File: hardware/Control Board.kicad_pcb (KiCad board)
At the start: 2 copper layers, 68.4 x 53.1 mm, 42 parts, among them J1 Conn_FTDI, J2 SOLAR, M1 MOTOR, Q1 IRF7105PbF, Q2 BC817W, Q3 BC817W, Q4 IRF7105PbF, SW1 SW_Push, SW2 SW_Push, SW3 SW_Push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

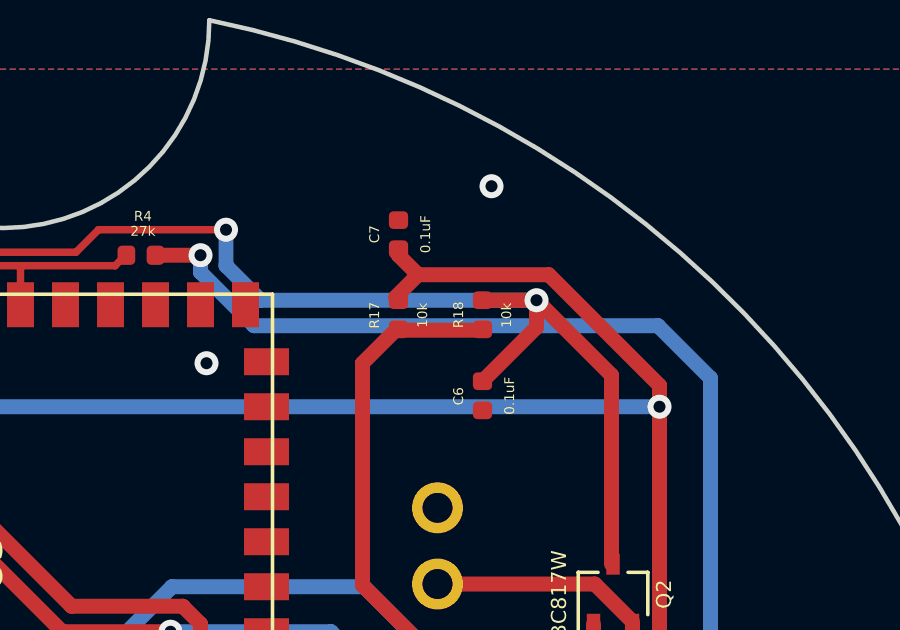
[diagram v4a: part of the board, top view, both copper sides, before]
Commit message: Placing the pull ups on the programmer
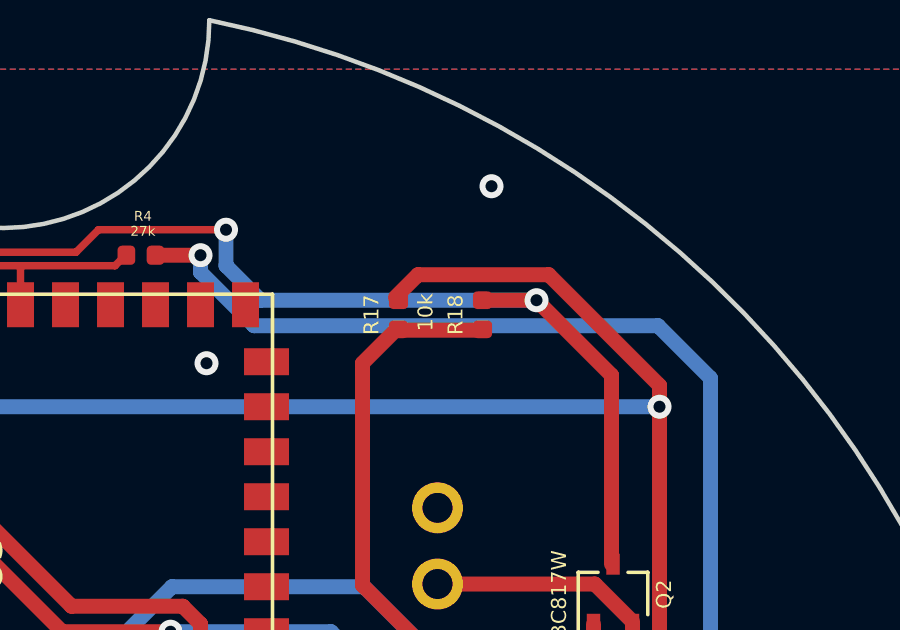
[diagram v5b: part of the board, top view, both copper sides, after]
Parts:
- removed C6, C7: 0.1uF, Capacitor_SMD:C_0402_1005Metric
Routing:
- net EN: track 53.0 -> 49.5 mm
- net IO0: track 72.7 -> 71.6 mm
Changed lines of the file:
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@@
     (thickness 1.6)
     (drawings 57)
-    (tracks 275)
+    (tracks 268)
     (zones 0)
-    (modules 42)
+    (modules 40)
     (nets 54)
   )
@@
     (tags resistor)
     (attr smd)
-    (fp_text reference R17 (at -0.015 -0.8 90) (layer F.SilkS)
-      (effects (font (size 0.33 0.33) (thickness 0.0825)))
-    )
-    (fp_text value 10k (at -0.015 0.8 90) (layer F.SilkS)
-      (effects (font (size 0.33 0.33) (thickness 0.0825)))
+    (fp_text reference R17 (at 0 -0.9 90) (layer F.SilkS)
+      (effects (font (size 0.5 0.5) (thickness 0.125)))
+    )
+    (fp_text value 10k (at 0.085 0.9 90) (layer F.SilkS)
+      (effects (font (size 0.5 0.5) (thickness 0.125)))
     )
     (fp_line (start 0.93 0.47) (end -0.93 0.47) (layer F.CrtYd) (width 0.05))
@@
     (tags resistor)
     (attr smd)
-    (fp_text reference R18 (at 0 -0.8 90) (layer F.SilkS)
-      (effects (font (size 0.33 0.33) (thickness 0.0825)))
-    )
-    (fp_text value 10k (at -0.015 0.8 90) (layer F.SilkS)
-      (effects (font (size 0.33 0.33) (thickness 0.0825)))
+    (fp_text reference R18 (at 0 -0.9 90) (layer F.SilkS)
+      (effects (font (size 0.5 0.5) (thickness 0.125)))
+    )
+    (fp_text value 10k (at 0.085 0.9 90) (layer B.Paste)
+      (effects (font (size 0.5 0.5) (thickness 0.125)))
     )
     (fp_text user %R (at 0 0 90) (layer F.Fab)
@@
       (net 3 +3V3))
     (model ${KISYS3DMOD}/Resistor_SMD.3dshapes/R_0402_1005Metric.wrl
-      (at (xyz 0 0 0))
-      (scale (xyz 1 1 1))
-      (rotate (xyz 0 0 0))
-    )
-  )
-  (module Capacitor_SMD:C_0402_1005Metric (layer F.Cu)
-    (at 125 109.385 270)
-    (descr "Capacitor SMD 0402 (1005 Metric), square (rectangular) end terminal, IPC_7351 nominal, (Body size source: http://www.tortai-tech.com/upload/download/2011102023233369053.pdf), generated with kicad-footprint-generator")
-    (tags capacitor)
-    (attr smd)
-    (fp_text reference C6 (at 0.015 0.8 90) (layer F.SilkS)
-      (effects (font (size 0.33 0.33) (thickness 0.0825)))
-    )
-    (fp_text value 0.1uF (at 0 -0.9 90) (layer F.SilkS)
-      (effects (font (size 0.33 0.33) (thickness 0.0825)))
-    )
-    (fp_line (start 0.93 0.47) (end -0.93 0.47) (layer F.CrtYd) (width 0.05))
-    (fp_line (start 0.93 -0.47) (end 0.93 0.47) (layer F.CrtYd) (width 0.05))
-    (fp_line (start -0.93 -0.47) (end 0.93 -0.47) (layer F.CrtYd) (width 0.05))
-    (fp_line (start -0.93 0.47) (end -0.93 -0.47) (layer F.CrtYd) (width 0.05))
-    (fp_line (start 0.5 0.25) (end -0.5 0.25) (layer F.Fab) (width 0.1))
-    (fp_line (start 0.5 -0.25) (end 0.5 0.25) (layer F.Fab) (width 0.1))
-    (fp_line (start -0.5 -0.25) (end 0.5 -0.25) (layer F.Fab) (width 0.1))
-    (fp_line (start -0.5 0.25) (end -0.5 -0.25) (layer F.Fab) (width 0.1))
-    (fp_text user %R (at 0 0 90) (layer F.Fab)
-      (effects (font (size 0.25 0.25) (thickness 0.04)))
-    )
-    (pad 1 smd roundrect (at -0.485 0 270) (size 0.59 0.64) (layers F.Cu F.Paste F.Mask) (roundrect_rratio 0.25)
-      (net 9 EN))
-    (pad 2 smd roundrect (at 0.485 0 270) (size 0.59 0.64) (layers F.Cu F.Paste F.Mask) (roundrect_rratio 0.25)
-      (net 1 GND))
-    (model ${KISYS3DMOD}/Capacitor_SMD.3dshapes/C_0402_1005Metric.wrl
-      (at (xyz 0 0 0))
-      (scale (xyz 1 1 1))
-      (rotate (xyz 0 0 0))
-    )
-  )
-  (module Capacitor_SMD:C_0402_1005Metric (layer F.Cu)
-    (at 122.2 104.015 90)
-    (descr "Capacitor SMD 0402 (1005 Metric), square (rectangular) end terminal, IPC_7351 nominal, (Body size source: http://www.tortai-tech.com/upload/download/2011102023233369053.pdf), generated with kicad-footprint-generator")
-    (tags capacitor)
-    (attr smd)
-    (fp_text reference C7 (at 0.015 -0.8 90) (layer F.SilkS)
-      (effects (font (size 0.33 0.33) (thickness 0.0825)))
-    )
-    (fp_text value 0.1uF (at 0.015 0.9 90) (layer F.SilkS)
-      (effects (font (size 0.33 0.33) (thickness 0.0825)))
-    )
-    (fp_text user %R (at 0 0 90) (layer F.Fab)
-      (effects (font (size 0.25 0.25) (thickness 0.04)))
-    )
-    (fp_line (start -0.5 0.25) (end -0.5 -0.25) (layer F.Fab) (width 0.1))
-    (fp_line (start -0.5 -0.25) (end 0.5 -0.25) (layer F.Fab) (width 0.1))
-    (fp_line (start 0.5 -0.25) (end 0.5 0.25) (layer F.Fab) (width 0.1))
-    (fp_line (start 0.5 0.25) (end -0.5 0.25) (layer F.Fab) (width 0.1))
-    (fp_line (start -0.93 0.47) (end -0.93 -0.47) (layer F.CrtYd) (width 0.05))
-    (fp_line (start -0.93 -0.47) (end 0.93 -0.47) (layer F.CrtYd) (width 0.05))
-    (fp_line (start 0.93 -0.47) (end 0.93 0.47) (layer F.CrtYd) (width 0.05))
-    (fp_line (start 0.93 0.47) (end -0.93 0.47) (layer F.CrtYd) (width 0.05))
-    (pad 2 smd roundrect (at 0.485 0 90) (size 0.59 0.64) (layers F.Cu F.Paste F.Mask) (roundrect_rratio 0.25)
-      (net 1 GND))
-    (pad 1 smd roundrect (at -0.485 0 90) (size 0.59 0.64) (layers F.Cu F.Paste F.Mask) (roundrect_rratio 0.25)
-      (net 10 IO0))
-    (model ${KISYS3DMOD}/Capacitor_SMD.3dshapes/C_0402_1005Metric.wrl
       (at (xyz 0 0 0))
       (scale (xyz 1 1 1))
@@
   (segment (start 106.4 104.6) (end 111.449999 104.6) (width 0.25) (layer F.Cu) (net 9))
   (segment (start 125 106.2) (end 126.8 106.2) (width 0.5) (layer F.Cu) (net 9))
-  (segment (start 126.8 107.1) (end 126.8 106.2) (width 0.5) (layer F.Cu) (net 9))
-  (segment (start 125 108.9) (end 126.8 107.1) (width 0.5) (layer F.Cu) (net 9))
   (via (at 130.9 109.75) (size 0.8) (drill 0.4) (layers F.Cu B.Cu) (net 10))
   (via (at 97.6 118.9) (size 0.8) (drill 0.4) (layers F.Cu B.Cu) (net 10))
@@
   (segment (start 130.9 109.75) (end 130.9 109.041998) (width 0.5) (layer F.Cu) (net 10))
   (segment (start 122.850001 105.349999) (end 122.1 106.1) (width 0.5) (layer F.Cu) (net 10))
-  (segment (start 122.2 104.699998) (end 122.850001 105.349999) (width 0.5) (layer F.Cu) (net 10))
-  (segment (start 122.2 104.5) (end 122.2 104.699998) (width 0.5) (layer F.Cu) (net 10))
   (segment (start 128.7 119.87) (end 128.7 121.8) (width 0.5) (layer F.Cu) (net 11))
   (segment (start 123.5 125.82) (end 124.58 125.82) (width 0.5) (layer F.Cu) (net 11))

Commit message: Broke the pcb during a merge.
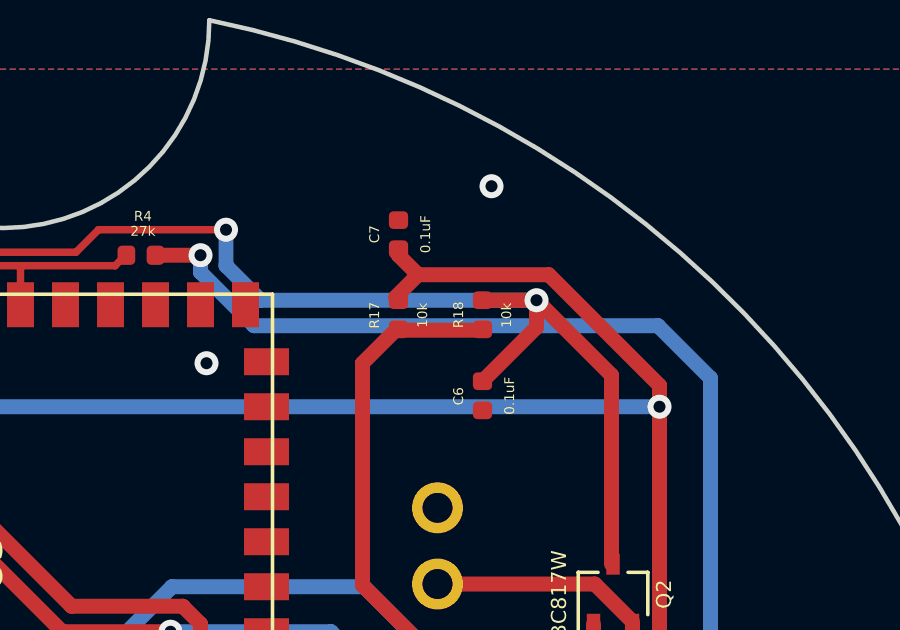
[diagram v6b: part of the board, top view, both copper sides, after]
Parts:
- added C6: 0.1uF, Capacitor_SMD:C_0402_1005Metric, F.Cu at (125.0, 109.4)
- added C7: 0.1uF, Capacitor_SMD:C_0402_1005Metric, F.Cu at (122.2, 104.0)
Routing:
- net EN: track 49.5 -> 53.0 mm
- net IO0: track 71.6 -> 72.7 mm
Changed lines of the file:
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@@
     (thickness 1.6)
     (drawings 57)
-    (tracks 268)
+    (tracks 275)
     (zones 0)
-    (modules 40)
+    (modules 42)
     (nets 54)
   )
@@
     (tags resistor)
     (attr smd)
-    (fp_text reference R17 (at 0 -0.9 90) (layer F.SilkS)
-      (effects (font (size 0.5 0.5) (thickness 0.125)))
-    )
-    (fp_text value 10k (at 0.085 0.9 90) (layer F.SilkS)
-      (effects (font (size 0.5 0.5) (thickness 0.125)))
+    (fp_text reference R17 (at -0.015 -0.8 90) (layer F.SilkS)
+      (effects (font (size 0.33 0.33) (thickness 0.0825)))
+    )
+    (fp_text value 10k (at -0.015 0.8 90) (layer F.SilkS)
+      (effects (font (size 0.33 0.33) (thickness 0.0825)))
     )
     (fp_line (start 0.93 0.47) (end -0.93 0.47) (layer F.CrtYd) (width 0.05))
@@
     (tags resistor)
     (attr smd)
-    (fp_text reference R18 (at 0 -0.9 90) (layer F.SilkS)
-      (effects (font (size 0.5 0.5) (thickness 0.125)))
-    )
-    (fp_text value 10k (at 0.085 0.9 90) (layer B.Paste)
-      (effects (font (size 0.5 0.5) (thickness 0.125)))
+    (fp_text reference R18 (at 0 -0.8 90) (layer F.SilkS)
+      (effects (font (size 0.33 0.33) (thickness 0.0825)))
+    )
+    (fp_text value 10k (at -0.015 0.8 90) (layer F.SilkS)
+      (effects (font (size 0.33 0.33) (thickness 0.0825)))
     )
     (fp_text user %R (at 0 0 90) (layer F.Fab)
@@
       (net 3 +3V3))
     (model ${KISYS3DMOD}/Resistor_SMD.3dshapes/R_0402_1005Metric.wrl
+      (at (xyz 0 0 0))
+      (scale (xyz 1 1 1))
+      (rotate (xyz 0 0 0))
+    )
+  )
+  (module Capacitor_SMD:C_0402_1005Metric (layer F.Cu)
+    (at 125 109.385 270)
+    (descr "Capacitor SMD 0402 (1005 Metric), square (rectangular) end terminal, IPC_7351 nominal, (Body size source: http://www.tortai-tech.com/upload/download/2011102023233369053.pdf), generated with kicad-footprint-generator")
+    (tags capacitor)
+    (attr smd)
+    (fp_text reference C6 (at 0.015 0.8 90) (layer F.SilkS)
+      (effects (font (size 0.33 0.33) (thickness 0.0825)))
+    )
+    (fp_text value 0.1uF (at 0 -0.9 90) (layer F.SilkS)
+      (effects (font (size 0.33 0.33) (thickness 0.0825)))
+    )
+    (fp_line (start 0.93 0.47) (end -0.93 0.47) (layer F.CrtYd) (width 0.05))
+    (fp_line (start 0.93 -0.47) (end 0.93 0.47) (layer F.CrtYd) (width 0.05))
+    (fp_line (start -0.93 -0.47) (end 0.93 -0.47) (layer F.CrtYd) (width 0.05))
+    (fp_line (start -0.93 0.47) (end -0.93 -0.47) (layer F.CrtYd) (width 0.05))
+    (fp_line (start 0.5 0.25) (end -0.5 0.25) (layer F.Fab) (width 0.1))
+    (fp_line (start 0.5 -0.25) (end 0.5 0.25) (layer F.Fab) (width 0.1))
+    (fp_line (start -0.5 -0.25) (end 0.5 -0.25) (layer F.Fab) (width 0.1))
+    (fp_line (start -0.5 0.25) (end -0.5 -0.25) (layer F.Fab) (width 0.1))
+    (fp_text user %R (at 0 0 90) (layer F.Fab)
+      (effects (font (size 0.25 0.25) (thickness 0.04)))
+    )
+    (pad 1 smd roundrect (at -0.485 0 270) (size 0.59 0.64) (layers F.Cu F.Paste F.Mask) (roundrect_rratio 0.25)
+      (net 9 EN))
+    (pad 2 smd roundrect (at 0.485 0 270) (size 0.59 0.64) (layers F.Cu F.Paste F.Mask) (roundrect_rratio 0.25)
+      (net 1 GND))
+    (model ${KISYS3DMOD}/Capacitor_SMD.3dshapes/C_0402_1005Metric.wrl
+      (at (xyz 0 0 0))
+      (scale (xyz 1 1 1))
+      (rotate (xyz 0 0 0))
+    )
+  )
+  (module Capacitor_SMD:C_0402_1005Metric (layer F.Cu)
+    (at 122.2 104.015 90)
+    (descr "Capacitor SMD 0402 (1005 Metric), square (rectangular) end terminal, IPC_7351 nominal, (Body size source: http://www.tortai-tech.com/upload/download/2011102023233369053.pdf), generated with kicad-footprint-generator")
+    (tags capacitor)
+    (attr smd)
+    (fp_text reference C7 (at 0.015 -0.8 90) (layer F.SilkS)
+      (effects (font (size 0.33 0.33) (thickness 0.0825)))
+    )
+    (fp_text value 0.1uF (at 0.015 0.9 90) (layer F.SilkS)
+      (effects (font (size 0.33 0.33) (thickness 0.0825)))
+    )
+    (fp_text user %R (at 0 0 90) (layer F.Fab)
+      (effects (font (size 0.25 0.25) (thickness 0.04)))
+    )
+    (fp_line (start -0.5 0.25) (end -0.5 -0.25) (layer F.Fab) (width 0.1))
+    (fp_line (start -0.5 -0.25) (end 0.5 -0.25) (layer F.Fab) (width 0.1))
+    (fp_line (start 0.5 -0.25) (end 0.5 0.25) (layer F.Fab) (width 0.1))
+    (fp_line (start 0.5 0.25) (end -0.5 0.25) (layer F.Fab) (width 0.1))
+    (fp_line (start -0.93 0.47) (end -0.93 -0.47) (layer F.CrtYd) (width 0.05))
+    (fp_line (start -0.93 -0.47) (end 0.93 -0.47) (layer F.CrtYd) (width 0.05))
+    (fp_line (start 0.93 -0.47) (end 0.93 0.47) (layer F.CrtYd) (width 0.05))
+    (fp_line (start 0.93 0.47) (end -0.93 0.47) (layer F.CrtYd) (width 0.05))
+    (pad 2 smd roundrect (at 0.485 0 90) (size 0.59 0.64) (layers F.Cu F.Paste F.Mask) (roundrect_rratio 0.25)
+      (net 1 GND))
+    (pad 1 smd roundrect (at -0.485 0 90) (size 0.59 0.64) (layers F.Cu F.Paste F.Mask) (roundrect_rratio 0.25)
+      (net 10 IO0))
+    (model ${KISYS3DMOD}/Capacitor_SMD.3dshapes/C_0402_1005Metric.wrl
       (at (xyz 0 0 0))
       (scale (xyz 1 1 1))
@@
   (segment (start 106.4 104.6) (end 111.449999 104.6) (width 0.25) (layer F.Cu) (net 9))
   (segment (start 125 106.2) (end 126.8 106.2) (width 0.5) (layer F.Cu) (net 9))
+  (segment (start 126.8 107.1) (end 126.8 106.2) (width 0.5) (layer F.Cu) (net 9))
+  (segment (start 125 108.9) (end 126.8 107.1) (width 0.5) (layer F.Cu) (net 9))
   (via (at 130.9 109.75) (size 0.8) (drill 0.4) (layers F.Cu B.Cu) (net 10))
   (via (at 97.6 118.9) (size 0.8) (drill 0.4) (layers F.Cu B.Cu) (net 10))
@@
   (segment (start 130.9 109.75) (end 130.9 109.041998) (width 0.5) (layer F.Cu) (net 10))
   (segment (start 122.850001 105.349999) (end 122.1 106.1) (width 0.5) (layer F.Cu) (net 10))
+  (segment (start 122.2 104.699998) (end 122.850001 105.349999) (width 0.5) (layer F.Cu) (net 10))
+  (segment (start 122.2 104.5) (end 122.2 104.699998) (width 0.5) (layer F.Cu) (net 10))
   (segment (start 128.7 119.87) (end 128.7 121.8) (width 0.5) (layer F.Cu) (net 11))
   (segment (start 123.5 125.82) (end 124.58 125.82) (width 0.5) (layer F.Cu) (net 11))

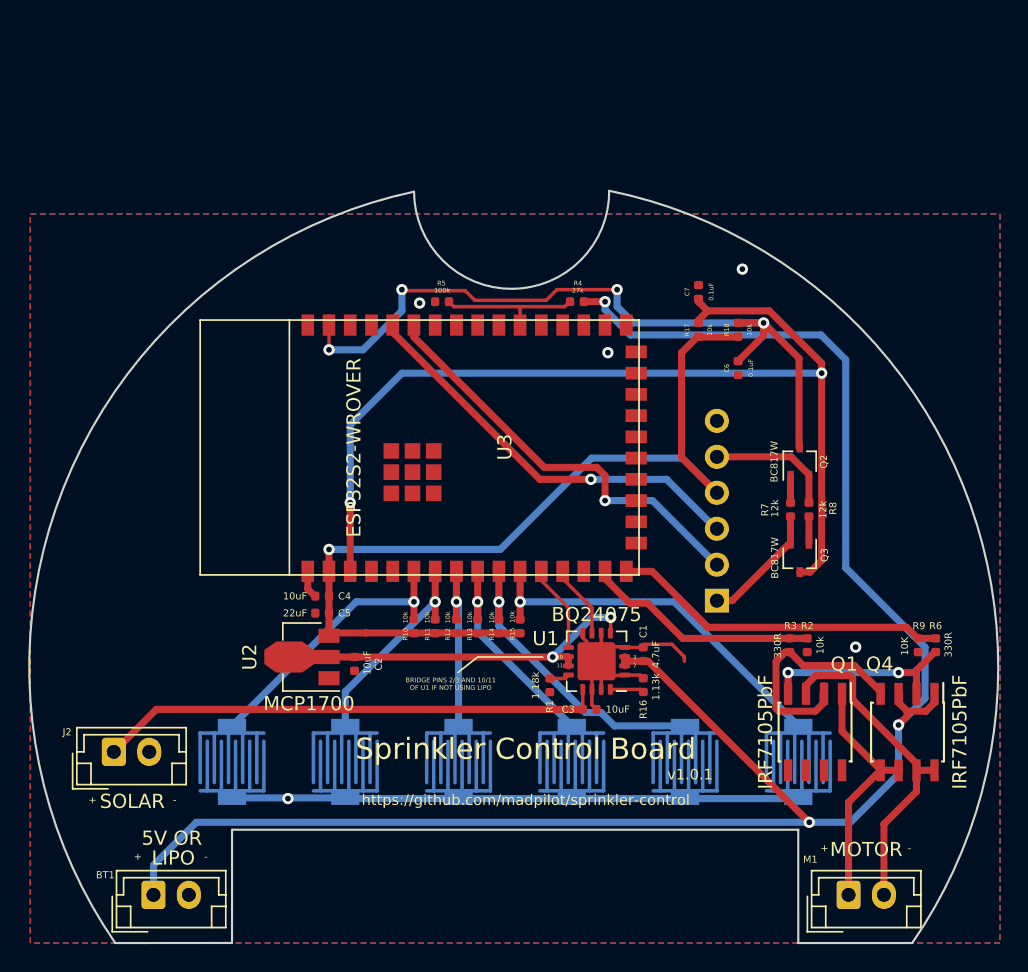
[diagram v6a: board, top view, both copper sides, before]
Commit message: Using 5V FTDI, adding protection diodes to allow dual power, adding some additional bypass caps
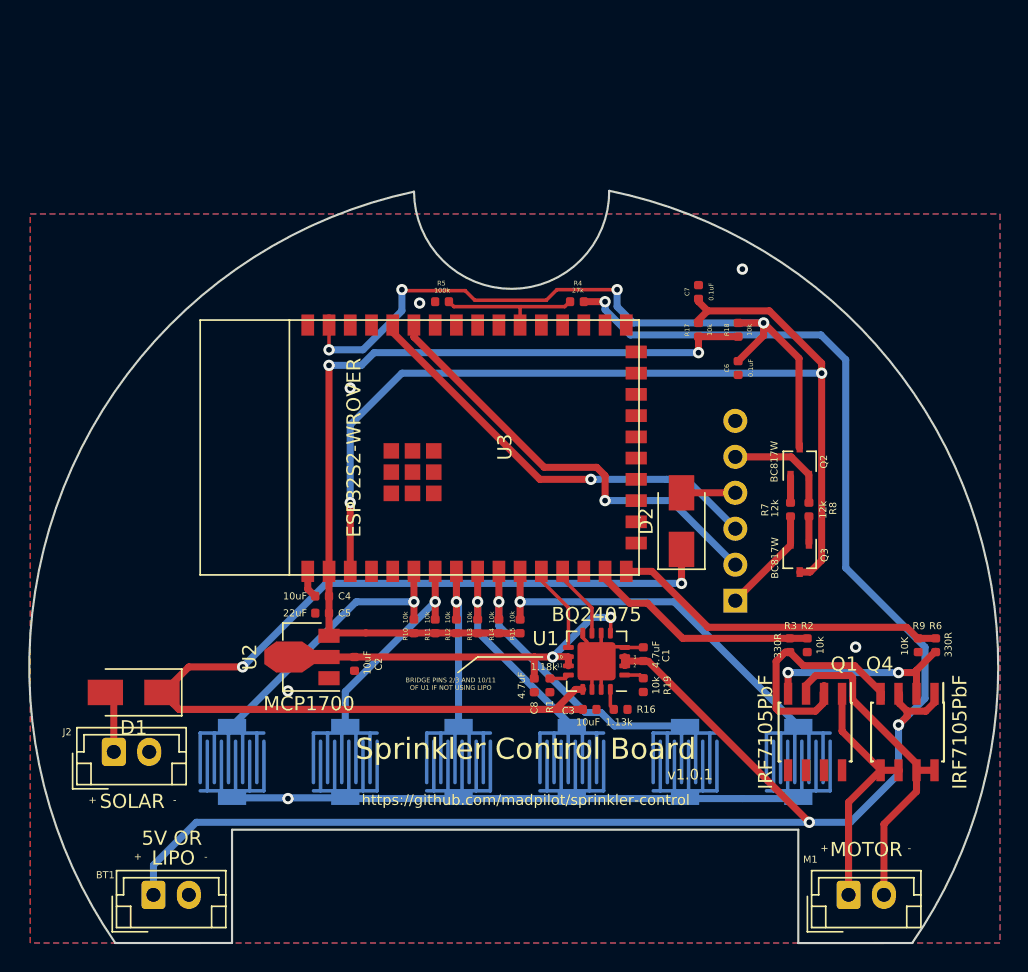
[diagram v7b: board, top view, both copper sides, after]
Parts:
- added C8: 4.7uF, Capacitor_SMD:C_0402_1005Metric, F.Cu at (110.6, 131.8)
- added D1: SK34A, Diode_SMD:D_SMA, F.Cu at (82.3, 132.3)
- added D2: SK34A, Diode_SMD:D_SMA, F.Cu at (121.0, 120.2)
- added R19: 10k, Resistor_SMD:R_0402_1005Metric, F.Cu at (118.3, 131.8)
- moved R16 2.35 mm to (116.7, 133.5), turned to 0 degrees
- moved J1 1.30 mm to (124.8, 125.8)
- turned C3 to 180 degrees
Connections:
- C3 pad 1: Net-(C3-Pad1) -> GND
- C3 pad 2: GND -> Net-(C3-Pad2)
- J1 pad 4: +3V3 -> +5V
- J2 pad 1: Net-(C3-Pad1) -> Net-(D1-Pad2)
- U1 pad 1: GND -> Net-(R19-Pad1)
- U1 pad 13: Net-(C3-Pad1) -> Net-(C3-Pad2)
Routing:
- net Net-(C3-Pad2): track 0.00 -> 76.0 mm, vias 0 -> 2
- net Net-(C3-Pad1): track 35.8 -> 0.00 mm
- net GND: track 62.9 -> 55.4 mm, vias 5 -> 6
- net Net-(D1-Pad2): track 0.00 -> 4.35 mm
- net +5V: track 0.00 -> 3.80 mm
- net +3V3: track 66.2 -> 63.0 mm, vias 1 -> 2
- net Net-(C2-Pad1): track 27.8 -> 29.3 mm
- net Net-(R19-Pad1): track 0.00 -> 1.41 mm
- net Net-(J1-Pad1): track 8.84 -> 7.47 mm
- net RX: track 29.9 -> 31.2 mm
- net Net-(J1-Pad5): track 8.92 -> 7.62 mm
- net TX: track 29.6 -> 30.9 mm
- net Net-(R16-Pad1): track 2.41 -> 1.19 mm
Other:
- board text added: "5V"
- board text removed: "3V3"
